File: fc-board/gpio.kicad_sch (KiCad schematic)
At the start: 29 parts, among them J6 10067847-001RLF, U1 749023310, U2 74LVC1G07SE-7, U7 RT9742GGJ5, X1 microSD_Card

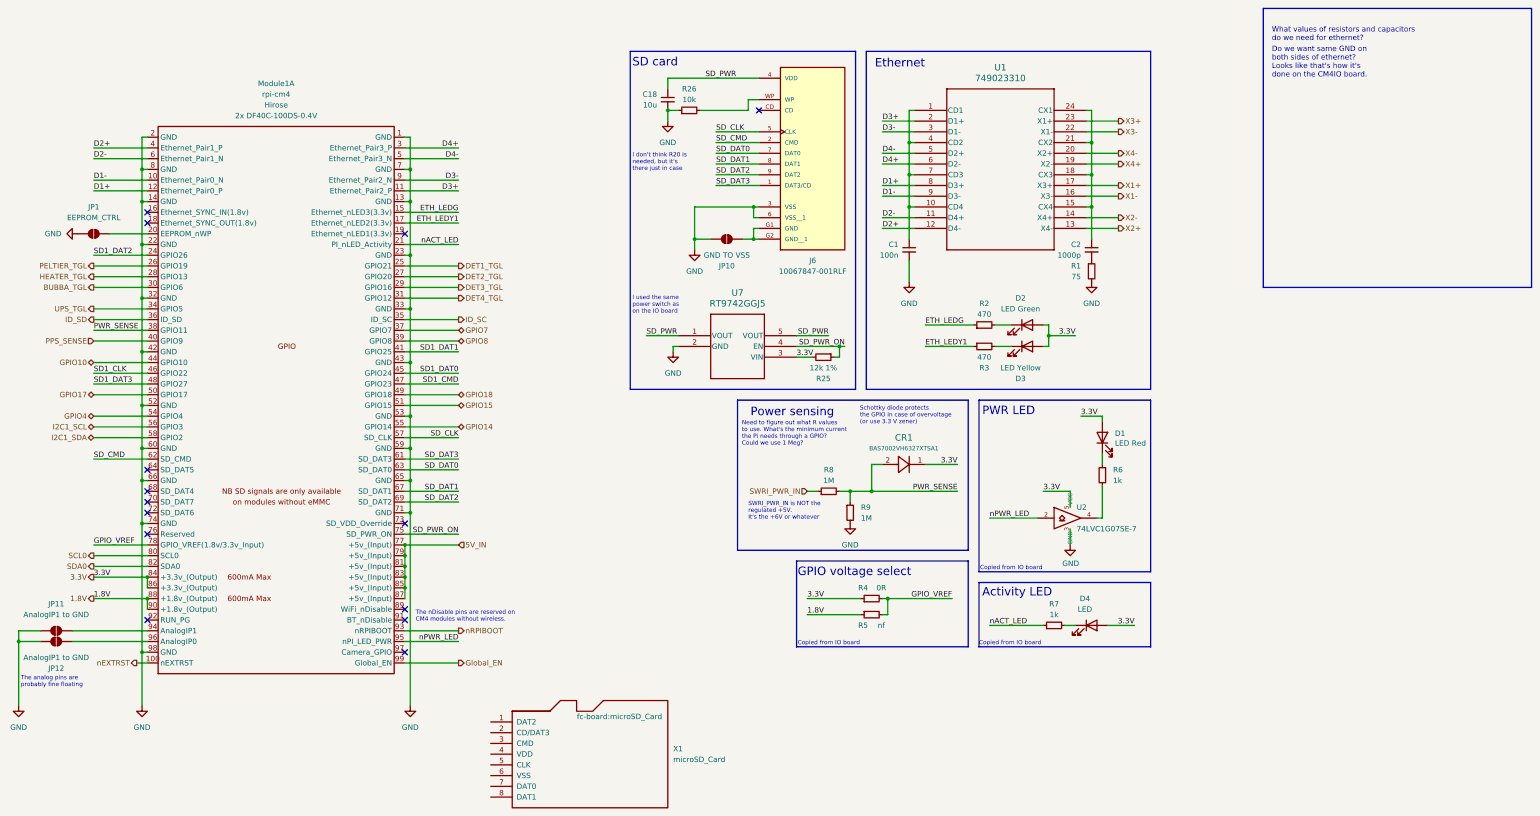
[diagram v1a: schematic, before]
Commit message: Removed zips; updated gitignore
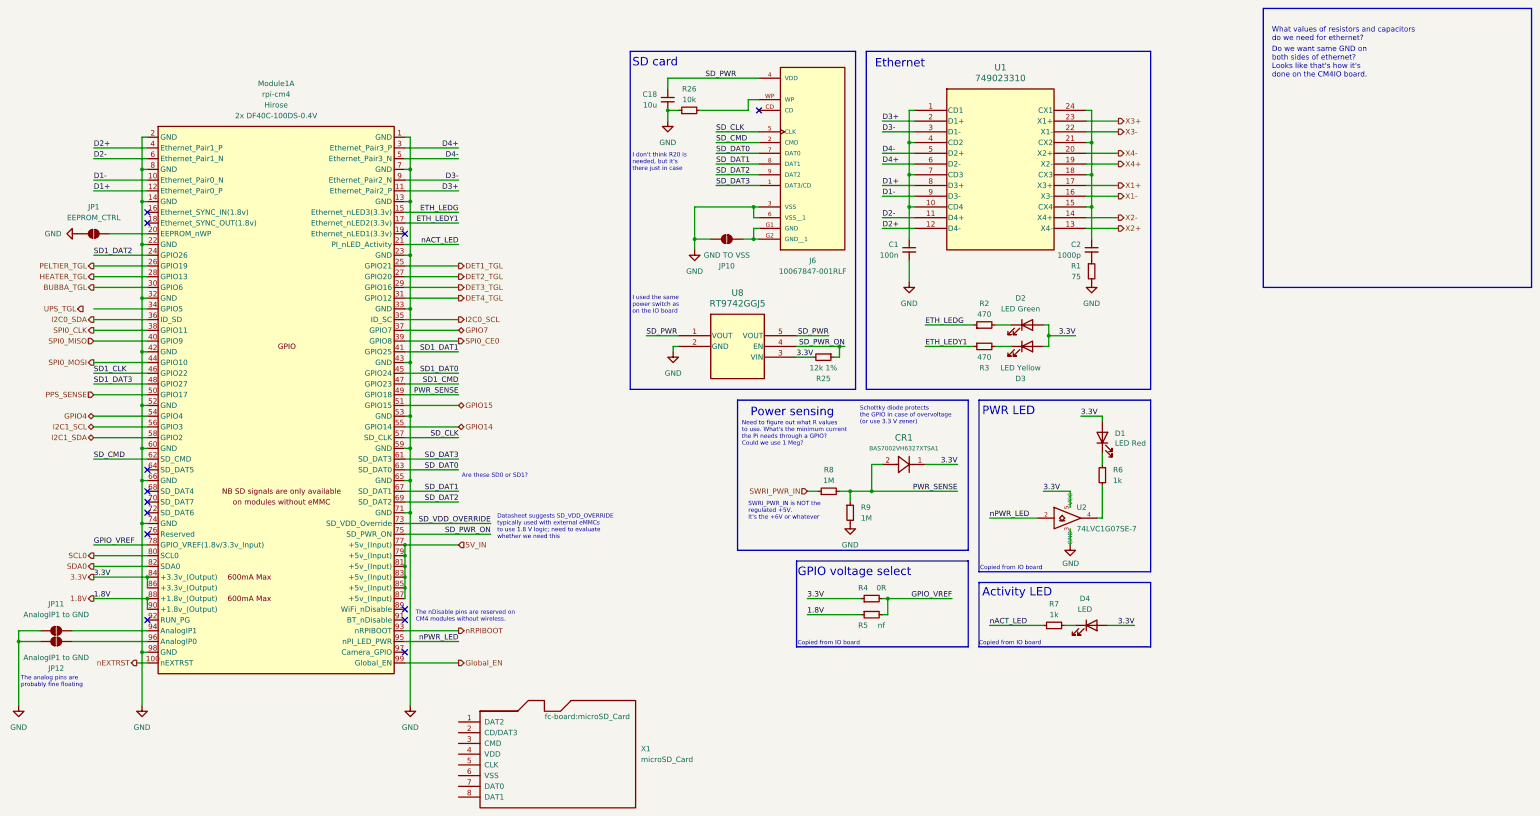
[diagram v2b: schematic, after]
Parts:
- renumbered U7 to U8
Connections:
- net GPIO17 is gone; now on net PPS_SENSE: Module1.50 (GPIO17)
- net GPIO18 is gone; now on net PWR_SENSE: Module1.49 (GPIO18)
- net PPS_SENSE: no longer Module1.40 (GPIO9)
- net PWR_SENSE: no longer Module1.38 (GPIO11)
- net UPS_TGL: no longer Module1.34 (GPIO5)
- net SD_VDD_OVERRIDE: now reaches Module1.73 (SD_VDD_Override)
- net GPIO10 renamed SPI0_MOSI
- net GPIO8 renamed SPI0_CE0
- net ID_SC renamed I2C0_SCL
- net ID_SD renamed I2C0_SDA
- new net SPI0_CLK: Module1.38 (GPIO11)
- new net SPI0_MISO: Module1.40 (GPIO9)
- no-connect marks 14 -> 13
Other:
- note added: "Are these SD0 or SD1?"
- note added: "Datasheet suggests SD_VDD_OVERRIDE typically used with external eMMCs to use 1.8 V logic; need to evaluate whether we need this"
- moved on the sheet: X1
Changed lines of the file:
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@@
 		)
 	)
+	(text "Datasheet suggests SD_VDD_OVERRIDE\ntypically used with external eMMCs\nto use 1.8 V logic; need to evaluate\nwhether we need this"
+		(exclude_from_sim no)
+		(at 127.254 130.81 0)
+		(effects
+			(font
+				(size 1 1)
+			)
+			(justify left bottom)
+		)
+	)
 	(text "Power sensing"
 		(exclude_from_sim no)
@@
 		)
 	)
+	(text "Are these SD0 or SD1?"
+		(exclude_from_sim no)
+		(at 118.872 116.332 0)
+		(effects
+			(font
+				(size 1 1)
+			)
+			(justify left bottom)
+		)
+	)
 	(text "Copied from IO board"
 		(exclude_from_sim no)
@@
 	)
 	(no_connect
-		(at 105.41 127)
-	)
-	(no_connect
 		(at 105.41 58.42)
 	)
@@
 	(wire
 		(pts
+			(xy 105.41 127) (xy 125.73 127)
+		)
+		(stroke
+			(width 0)
+			(type default)
+		)
+	)
+	(wire
+		(pts
 			(xy 266.7 46.99) (xy 274.32 46.99)
 		)
@@
 	(wire
 		(pts
-			(xy 105.41 129.54) (xy 118.11 129.54)
+			(xy 105.41 129.54) (xy 125.73 129.54)
 		)
 		(stroke
@@
 	)
 	(label "PWR_SENSE"
-		(at 31.75 81.28 0)
+		(at 118.11 96.52 180)
 		(effects
 			(font
 				(size 1.27 1.27)
 			)
-			(justify left bottom)
+			(justify right bottom)
 		)
 	)
@@
 		)
 	)
+	(label "SD_VDD_OVERRIDE"
+		(at 125.73 127 180)
+		(effects
+			(font
+				(size 1.27 1.27)
+			)
+			(justify right bottom)
+		)
+	)
 	(label "SD1_DAT3"
 		(at 31.75 93.98 0)
@@
 	)
 	(label "SD_PWR_ON"
-		(at 118.11 129.54 180)
+		(at 125.73 129.54 180)
 		(effects
 			(font
@@
 		)
 	)
-	(hierarchical_label "ID_SC"
+	(hierarchical_label "I2C0_SCL"
 		(shape output)
 		(at 118.11 78.74 0)
@@
 		)
 	)
-	(hierarchical_label "GPIO17"
-		(shape bidirectional)
-		(at 31.75 96.52 180)
+	(hierarchical_label "PELTIER_TGL"
+		(shape output)
+		(at 31.75 66.04 180)
 		(effects
 			(font
@@
 		)
 	)
-	(hierarchical_label "PELTIER_TGL"
+	(hierarchical_label "X3+"
 		(shape output)
-		(at 31.75 66.04 180)
+		(at 274.32 31.75 0)
 		(effects
 			(font
 				(size 1.27 1.27)
 			)
-			(justify right)
+			(justify left)
 		)
 	)
-	(hierarchical_label "X3+"
+	(hierarchical_label "SPI0_CLK"
 		(shape output)
-		(at 274.32 31.75 0)
+		(at 31.75 81.28 180)
 		(effects
 			(font
 				(size 1.27 1.27)
 			)
-			(justify left)
+			(justify right)
+		)
+	)
+	(hierarchical_label "SPI0_MISO"
+		(shape input)
+		(at 31.75 83.82 180)
+		(effects
+			(font
+				(size 1.27 1.27)
+			)
+			(justify right)
 		)
 	)
@@
 		)
 	)
-	(hierarchical_label "ID_SD"
+	(hierarchical_label "I2C0_SDA"
 		(shape output)
 		(at 31.75 78.74 180)
@@
 		)
 	)
-	(hierarchical_label "GPIO10"
-		(shape bidirectional)
-		(at 31.75 88.9 180)
-		(effects
-			(font
-				(size 1.27 1.27)
-			)
-			(justify right)
-		)
-	)
 	(hierarchical_label "1.8V"
 		(shape output)
@@
 		)
 	)
-	(hierarchical_label "GPIO18"
-		(shape bidirectional)
-		(at 118.11 96.52 0)
-		(effects
-			(font
-				(size 1.27 1.27)
-			)
-			(justify left)
-		)
-	)
 	(hierarchical_label "HEATER_TGL"
 		(shape output)
@@
 		)
 	)
+	(hierarchical_label "SPI0_MOSI"
+		(shape output)
+		(at 31.75 88.9 180)
+		(effects
+			(font
+				(size 1.27 1.27)
+			)
+			(justify right)
+		)
+	)
 	(hierarchical_label "I2C1_SDA"
 		(shape bidirectional)
@@
 		)
 	)
+	(hierarchical_label "SPI0_CE0"
+		(shape output)
+		(at 118.11 83.82 0)
+		(effects
+			(font
+				(size 1.27 1.27)
+			)
+			(justify left)
+		)
+	)
 	(hierarchical_label "GPIO7"
 		(shape bidirectional)
@@
 	(hierarchical_label "PPS_SENSE"
 		(shape input)
-		(at 31.75 83.82 180)
+		(at 31.75 96.52 180)
 		(effects
 			(font
@@
 	(hierarchical_label "UPS_TGL"
 		(shape output)
-		(at 31.75 76.2 180)
+		(at 29.21 76.2 180)
 		(effects
 			(font
@@
 		)
 	)
-	(hierarchical_label "GPIO8"
-		(shape bidirectional)
-		(at 118.11 83.82 0)
-		(effects
-			(font
-				(size 1.27 1.27)
-			)
-			(justify left)
-		)
-	)
 	(hierarchical_label "nRPIBOOT"
 		(shape output)
@@
 			)
 		)
+		(property "Sim.Pins" "1=K 2=A"
+			(at 270.51 106.68 0)
+			(effects
+				(font
+					(size 1.27 1.27)
+				)
+				(hide yes)
+			)
+		)
 		(pin "1"
 		)
@@
 			)
 		)
+		(property "Sim.Pins" "1=K 2=A"
+			(at 252.73 80.01 0)
+			(effects
+				(font
+					(size 1.27 1.27)
+				)
+				(hide yes)
+			)
+		)
 		(pin "1"
 		)
@@
 	(symbol
 		(lib_id "microsd:microSD_Card")
-		(at 151.13 181.61 0)
+		(at 143.51 181.61 0)
 		(unit 1)
 		(exclude_from_sim no)
@@
 		(fields_autoplaced yes)
 		(property "Reference" "X1"
-			(at 168.91 180.3399 0)
+			(at 161.29 180.3399 0)
 			(effects
 				(font
@@
 		)
 		(property "Value" "microSD_Card"
-			(at 168.91 182.8799 0)
+			(at 161.29 182.8799 0)
 			(effects
 				(font
@@
 		)
 		(property "Footprint" "fc-board:microSD_Card"
-			(at 156.21 172.72 0)
+			(at 148.59 172.72 0)
 			(effects
 				(font
@@
 		)
 		(property "Datasheet" ""
-			(at 151.13 181.61 0)
+			(at 143.51 181.61 0)
 			(effects
 				(font
@@
 		)
 		(property "Description" ""
-			(at 151.13 181.61 0)
+			(at 143.51 181.61 0)
 			(effects
 				(font
@@
 		(on_board yes)
 		(dnp no)
-		(fields_autoplaced yes)
 		(property "Reference" "Module1"
 			(at 74.93 22.86 0)
@@
 		(dnp no)
 		(fields_autoplaced yes)
-		(property "Reference" "U7"
+		(property "Reference" "U8"
 			(at 184.15 72.39 0)
 			(effects
@@
 			(project ""
 				(path "/14bbabed-904f-4efc-8ba4-be00e59385c4/21f70e3e-098f-47c8-b8cd-a351aace6ca2"
-					(reference "U7")
+					(reference "U8")
 					(unit 1)
 				)
@@
 			)
 		)
+		(property "Sim.Pins" "1=K 2=A"
+			(at 252.73 85.09 0)
+			(effects
+				(font
+					(size 1.27 1.27)
+				)
+				(hide yes)
+			)
+		)
 		(pin "1"
 		)
@@
 			(at 267.97 151.13 0)
 			(effects
+				(font
+					(size 1.27 1.27)
+				)
+				(hide yes)
+			)
+		)
+		(property "Sim.Pins" "1=K 2=A"
+			(at 267.97 151.13 0)
+			(effects

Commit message: FC board updates
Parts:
- removed C18: 10u, Capacitor_SMD:C_1206_3216Metric, symbol Device:C_Small
- removed CR1: BAS7002VH6327XTSA1, fc-board:BAS7002VH6327XTSA1, symbol fc-board:BAS7002VH6327XTSA1
- removed J6: 10067847-001RLF, fc-board:10067847_001RLF, symbol fc-board:10067847-001RLF
- removed JP1: EEPROM_CTRL, Jumper:SolderJumper-2_P1.3mm_Open_Pad1.0x1.5mm, symbol Jumper:SolderJumper_2_Open
- removed JP10: GND TO VSS, Jumper:SolderJumper-2_P1.3mm_Open_Pad1.0x1.5mm, symbol Jumper:SolderJumper_2_Open
- removed JP11, JP12: AnalogIP1 to GND, Jumper:SolderJumper-2_P1.3mm_Open_Pad1.0x1.5mm, symbol Jumper:SolderJumper_2_Open
- removed R25: 12k 1%, Resistor_SMD:R_1206_3216Metric, symbol Device:R_Small
- removed R26: 10k, Resistor_SMD:R_1206_3216Metric, symbol Device:R_Small
- removed R8, R9: 1M, Resistor_SMD:R_1206_3216Metric, symbol Device:R_Small
- removed U2: 74LVC1G07SE-7, fc-board:74LVC1G07SE_7, symbol CM4IO:74LVC1G07_copy
- removed U8: RT9742GGJ5, fc-board:RT9742GGJ5, symbol fc-board:RT9742GGJ5
- removed X1: microSD_Card, fc-board:microSD_Card, symbol microsd:microSD_Card
- added C1, C2, C3: 10u, Capacitor_SMD:C_1206_3216Metric, symbol Device:C
- added J12: Micro_SD_Card_Det2, fc-board:molex-503398-1892, symbol Connector:Micro_SD_Card_Det2
- added JP2: AnalogIP1 to GND, Jumper:SolderJumper-2_P1.3mm_Open_Pad1.0x1.5mm, symbol Jumper:SolderJumper_2_Open
- added JP3: AnalogIP0 to GND, Jumper:SolderJumper-2_P1.3mm_Open_Pad1.0x1.5mm, symbol Jumper:SolderJumper_2_Open
- added JP4: EEPROM_CTRL, Jumper:SolderJumper-2_P1.3mm_Open_Pad1.0x1.5mm, symbol Jumper:SolderJumper_2_Open
- added R4, R5: nf, Resistor_SMD:R_1206_3216Metric_Pad1.30x1.75mm_HandSolder, symbol Device:R_Small
- added R6: 12k 1%, Resistor_SMD:R_1206_3216Metric, symbol Device:R_Small
- added U1: KS4GRI-806C-32, fc-board:KS4GRI-806C-32, symbol fc-board:KS4GRI-806C-32
- added U2: RT9742GGJ5, fc-board:RT9742GGJ5, symbol fc-board:RT9742GGJ5
- added U4: 74LVC1G07SE-7, fc-board:74LVC1G07SE_7, symbol fc-board:74LVC1G07SE-7
- added X1: microSD-card, fc-board:microSD-card, symbol fc-board:microSD-card
- C4: renamed from C1; footprint Capacitor_SMD:C_0805_2012Metric -> Capacitor_SMD:C_1206_3216Metric
- C5: renamed from C2; footprint Capacitor_SMD:C_0805_2012Metric -> Capacitor_SMD:C_1206_3216Metric
- R12: renamed from R1; footprint Resistor_SMD:R_0805_2012Metric -> Resistor_SMD:R_1206_3216Metric
- R7: renamed from R4; footprint Resistor_SMD:R_1206_3216Metric -> Resistor_SMD:R_1206_3216Metric_Pad1.30x1.75mm_HandSolder
- R8: renamed from R5; footprint Resistor_SMD:R_1206_3216Metric -> Resistor_SMD:R_1206_3216Metric_Pad1.30x1.75mm_HandSolder
- renumbered D2 to D1, D3 to D2, D4 to D3, D1 to D4, R3 to R10, R7 to R11, R6 to R13, R2 to R9, U1 to U3
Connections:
- net GPIO4 is gone; now on net DET1_TGL: Module1.54 (GPIO4)
- net GPIO7 is gone; now on net DET4_TGL: Module1.37 (GPIO7)
- net 3.3V: now also C1.1, C2.1, J12.4 (VDD), R4.1, R6.1, U1.B8 (VDD), U1.C5 (VDD), U1.G5 (VDD), U2.5 (VIN), U4.5 (VCC)
- net BUBBA_TGL: now also Module1.31 (GPIO12); no longer Module1.30 (GPIO6)
- net DET1_TGL: no longer Module1.25 (GPIO21)
- net DET2_TGL: now also Module1.34 (GPIO5); no longer Module1.27 (GPIO20)
- net DET3_TGL: now also Module1.30 (GPIO6); no longer Module1.29 (GPIO16)
- net DET4_TGL: no longer Module1.31 (GPIO12)
- net GND: now also C1.2, C2.2, C3.2, J12.11 (SHIELD), J12.6 (VSS), JP2.1 (A), JP3.1 (A), JP4.1 (A), U1.B1 (VSS), U1.C3 (VSS), U1.C6 (VSS), U1.G7 (VSS), U2.2 (GND), U4.3 (GND), X1.6 (VSS)
- net PPS_SENSE: now also Module1.29 (GPIO16); no longer Module1.50 (GPIO17)
- net SD1_CLK: now also X1.5 (CLK)
- net SD1_CMD: now also X1.3 (CMD)
- net SD1_DAT0: now also X1.7 (DAT0)
- net SD1_DAT1: now also X1.8 (DAT1)
- net SD1_DAT2: now also X1.1 (DAT2)
- net SD1_DAT3: now also X1.2 (CD/DAT3)
- net SD_CLK: now also J12.5 (CLK), U1.C4 (CLK)
- net SD_CMD: now also J12.3 (CMD), U1.C7 (CMD)
- net SD_DAT0: now also J12.7 (DAT0), U1.C2 (DAT0)
- net SD_DAT1: now also J12.8 (DAT1), U1.C1 (DAT1)
- net SD_DAT2: now also J12.1 (DAT2), U1.C9 (DAT2)
- net SD_DAT3: now also J12.2 (DAT3/CD), U1.C8 (CD/DAT3)
- net SD_PWR: now also C3.1, U2.1 (VOUT), X1.4 (VDD)
- net SD_PWR_ON: now also R6.2, U2.4 (EN)
- net nPWR_LED: now also U4.2
- net at Module1.20 (EEPROM_nWP): now also JP4.2 (B)
- net at R13.2: now also U4.4
- net at Module1.94 (AnalogIP1): now also JP2.2 (B)
- net at Module1.96 (AnalogIP0): now also JP3.2 (B)
- net GPIO14 renamed UART_TX
- net GPIO15 renamed UART_RX
- net PELTIER_TGL renamed GPIO19
- net PWR_SENSE renamed GPIO18
- new net: J12.10 (DET_A), R4.2
- new net: J12.9 (DET_B), R5.2
- new net GPIO17: Module1.50 (GPIO17)
- new net GPIO20: Module1.27 (GPIO20)
- new net GPIO21: Module1.25 (GPIO21)
- new net Reserved: R5.1
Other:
- note added: "According to raspi-gpio get on the CM4 Lite, SD_* are the SD0 interface"
- note added: "Data storage connected to the SD1 interface. Soldered directly to the PCB."
- note added: "MicroSD card"
- note added: "Modified from IO board"
- note added: "SDChip"
- note added: "This will be a backup for loading the OS in case we have issues with the Cactus SDChip. Connected to the SD0 interface."
- note added: "This will store the OS. Uses the SD0 interface."
- note removed: "Are these SD0 or SD1?"
- note removed: "I don't think R20 is needed, but it's there just in case"
- note removed: "I used the same power switch as on the IO board"
- note removed: "Need to figure out what R values to use. What's the minimum current the Pi needs through a GPIO? Could we use 1 Meg?"
- note removed: "Power sensing"
- note removed: "SD card"
- note removed: "SWRI_PWR_IN is NOT the regulated +5V. It's the +6V or whatever"
- note removed: "Schottky diode protects the GPIO in case of overvoltage (or use 3.3 V zener)"
- moved on the sheet: Module1A

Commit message: Finished routing; cleaned library
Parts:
- removed J12: Micro_SD_Card_Det2, fc-board:molex-503398-1892, symbol Connector:Micro_SD_Card_Det2
- removed R5: nf, Resistor_SMD:R_1206_3216Metric_Pad1.30x1.75mm_HandSolder, symbol Device:R_Small
- added J14: Micro_SD_Card_Det2, fc-board:molex-503398-1892, symbol fc-board:Micro_SD_Card_Det2
- renumbered C1 to C3, C2 to C4, C3 to C5, C4 to C6, C5 to C7, JP2 to JP4, JP3 to JP5, JP4 to JP6, R11 to R10, R12 to R11, R13 to R12, R6 to R5, R7 to R6, R8 to R7, R9 to R8, R10 to R9
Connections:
- net X4+ is gone; now on net X1-: U3.19 (X2-)
- net X4- is gone; now on net X1+: U3.20 (X2+)
- net 3.3V: now also J14.4 (VDD)
- net D1+: now also U3.5 (D2+); no longer U3.8 (D3+)
- net D1-: now also U3.6 (D2-); no longer U3.9 (D3-)
- net D2+: now also U3.9 (D3-); no longer U3.12 (D4-)
- net D2-: now also U3.8 (D3+); no longer U3.11 (D4+)
- net GND: now also J14.11 (SHIELD), J14.6 (VSS)
- net SD_CLK: now also J14.5 (CLK)
- net SD_CMD: now also J14.3 (CMD)
- net SD_DAT0: now also J14.7 (DAT0)
- net SD_DAT1: now also J14.8 (DAT1)
- net SD_DAT2: now also J14.1 (DAT2)
- net SD_DAT3: now also J14.2 (DAT3/CD)
- net X1+: no longer U3.17 (X3+)
- net X1-: no longer U3.16 (X3-)
- net X2+: now also U3.16 (X3-); no longer U3.13 (X4-)
- net X2-: now also U3.17 (X3+); no longer U3.14 (X4+)
- net at C7.1, U3.18 (CX3), U3.21 (CX2): no longer U3.15 (CX4), U3.24 (CX1)
- net at C6.1, U3.4 (CD2), U3.7 (CD3): no longer U3.1 (CD1), U3.10 (CD4)
- net at R4.2: now also J14.10 (DET_A)
- net D3+: no longer names the net of U3.2 (D1+)
- net D3+: no longer Module1.11 (Ethernet_Pair2_P)
- net D3-: no longer names the net of U3.3 (D1-)
- net D3-: no longer Module1.9 (Ethernet_Pair2_N)
- net D4+: no longer names the net of Module1.3 (Ethernet_Pair3_P)
- net D4+: no longer U3.6 (D2-)
- net D4-: no longer names the net of Module1.5 (Ethernet_Pair3_N)
- net D4-: no longer U3.5 (D2+)
- net SD_VDD_OVERRIDE: no longer names the net of Module1.73 (SD_VDD_Override)
- net X3+: no longer names the net of U3.23 (X1+)
- net X3-: no longer names the net of U3.22 (X1-)
- no-connect marks 13 -> 31

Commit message: Updated RJ45 jack
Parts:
- removed C4, C5: 10u, Capacitor_SMD:C_1206_3216Metric, symbol Device:C
- added C2, C3: 10u, Capacitor_SMD:C_1206_3216Metric, symbol Device:C
- C1: renamed from C3; Field4 Digikey -> (none); Field5 490-14381-1-ND -> (none); Field6 GRM21BR71A106KA73L -> (none); Field7 Murata -> (none); Field8 111893011 -> (none); Part Description 10uF 10% 10V Ceramic Capacitor X7R 0805 (2012 Metric) -> (none)
- D1: value LED Green -> LTST-S270KGKT
- D2: value LED Yellow -> LTST-S270KSKT
- D3: renamed from D4; value LED Red -> LTST-S270KRKT; Field4 Digikey -> (none); Field5 LTST-S270KRKT -> (none); Field6 SML-A12U8TT86Q -> (none); Field7 Rohm -> (none); Field8 650295101 -> (none); Part Description Red 620nm LED Indication - Discrete 2.2V 2-SMD, No Lead -> (none)
- D4: renamed from D3; value LED -> LTST-S270KGKT
- R6: value 0R -> 0
- R7: value nf -> 0
- renumbered C6 to C4, C7 to C5, J14 to J13
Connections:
- net 3.3V: now also C2.1
- net GND: now also C2.2, C3.2
- net SD_PWR: now also C3.1
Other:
- moved on the sheet: D1, D2, D3, D4, R10

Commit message: Assigned part numbers to everything, replaced ethernet jack
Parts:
- C4: value 100n -> 0.1u
- renumbered J13 to J14, JP4 to JP3, JP5 to JP4, JP6 to JP5
